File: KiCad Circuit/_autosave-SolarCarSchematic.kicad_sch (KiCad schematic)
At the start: 21 parts, among them Q1 BS250, Q2 NMOS, Q3 IPP060N06N, Q4 PMOS, U1 TL494

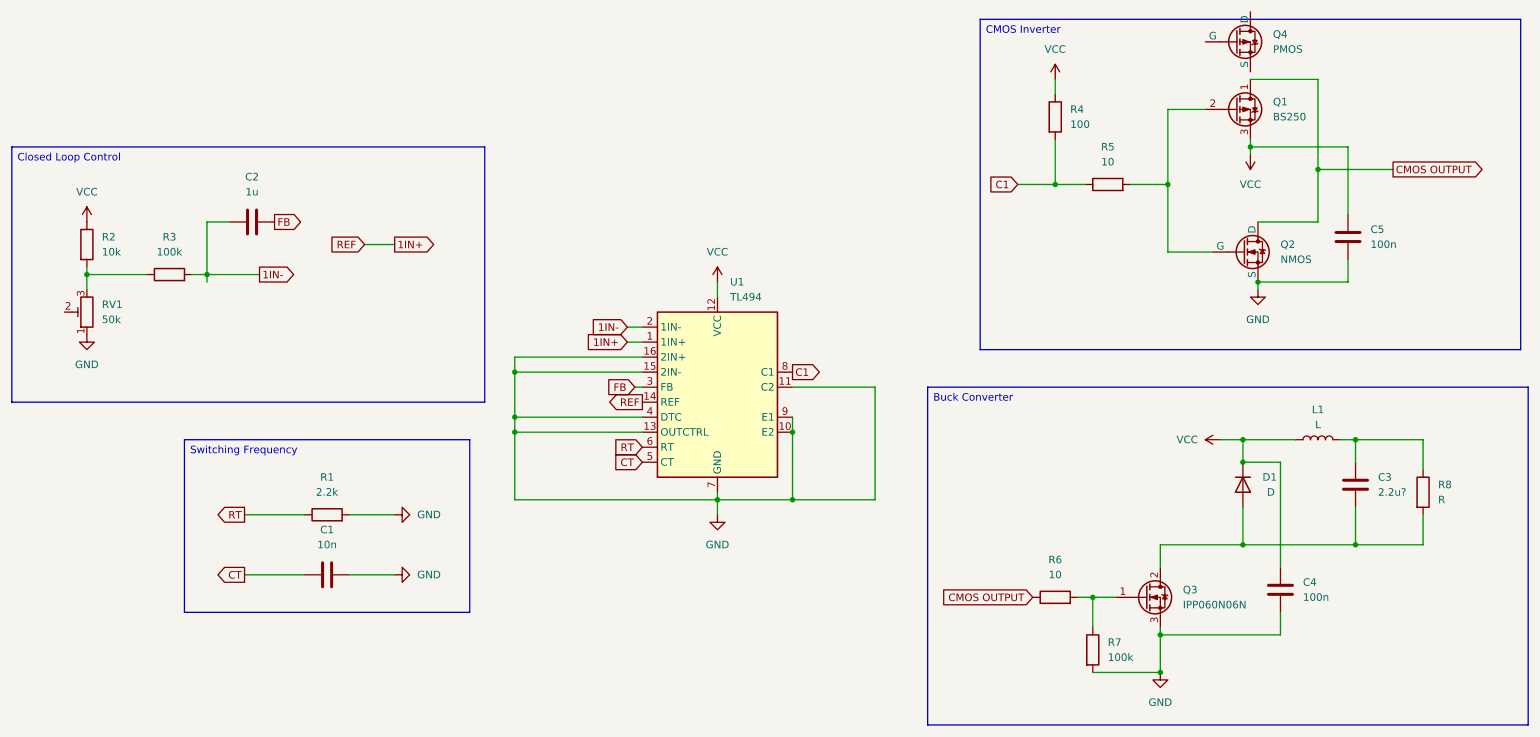
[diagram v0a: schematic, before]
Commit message: KiCad schematic with updated accurate values
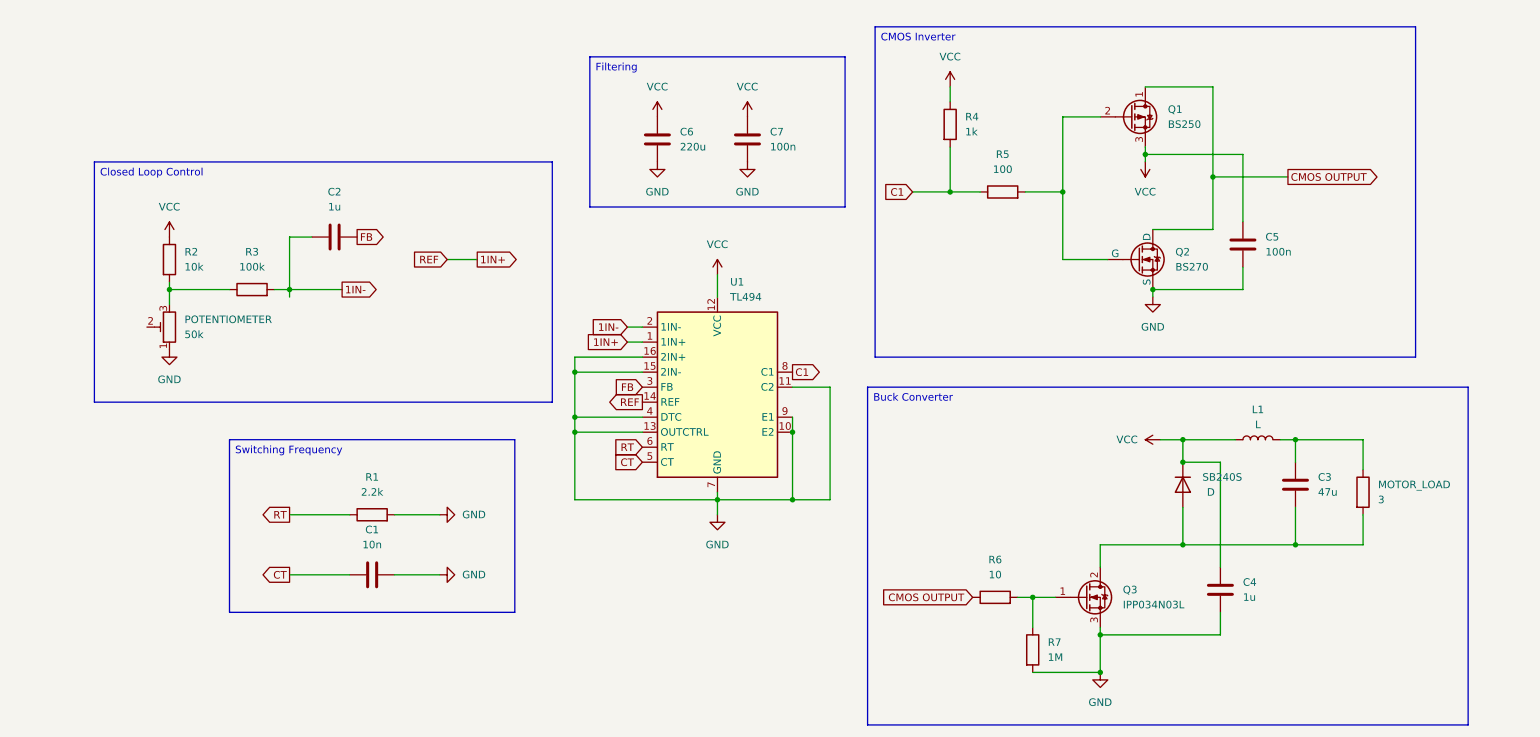
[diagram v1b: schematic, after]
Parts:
- removed Q4: PMOS, symbol Simulation_SPICE:PMOS
- added C6: 220u, symbol Device:C
- added C7: 100n, symbol Device:C
- C3: value 2.2u? -> 47u
- C4: value 100n -> 1u
- MOTOR_LOAD: renamed from R8; value R -> 3
- Q2: value NMOS -> BS270
- Q3: value IPP060N06N -> IPP034N03L
- R4: value 100 -> 1k
- R5: value 10 -> 100
- R7: value 100k -> 1M
- renumbered RV1 to POTENTIOMETER, D1 to SB240S
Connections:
- net GND: now also C6.2, C7.2
- net VCC: now also C6.1, C7.1
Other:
- title: (none) -> Solar Car Schematic
- moved on the sheet: C1, C2, C3, C4, C5, L1, MOTOR_LOAD, POTENTIOMETER, Q1, Q2, Q3, R1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
